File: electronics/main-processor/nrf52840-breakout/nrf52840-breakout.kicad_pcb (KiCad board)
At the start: 2 copper layers, 53 x 104.6 mm, 82 parts, among them J1 TBP02R2-381-03BE, J2 TBP02R2-381-02BE, J3 ST1W008S4AR1500, J4 TBP02R2-381-03BE, J5 USB4070-30-C_REVC5, J6 CONUFL001-SMD-T, J7 21992304, J8 Conn_01x04_Male, J9 TBP02R2-381-02BE, Q1 BSS214NW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

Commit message: up to pcb trace routing of circuit board, added boot and reset button
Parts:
- removed ?: , Micromod:M.2-CARD-E-22
- removed H1, H2: MountingHole, MountingHole:MountingHole_3.2mm_M3_Pad_Via
- removed JP1, JP2: SJ(Open), Jumper:SolderJumper-2_P1.3mm_Open_Pad1.0x1.5mm
- removed JP3, JP4: SJ(Clsd), Jumper:SolderJumper-2_P1.3mm_Bridged_Pad1.0x1.5mm
- added MP1: 9774025151R, 9774025151R:WE_9774025151R, F.Cu at (85.9, 110.6)
- added S2: RST, PTS636_SM43J_SMTR_LFS:SW_PTS636_SM43J_SMTR_LFS, F.Cu at (86.7, 96.8)
- added S3: BOOT, PTS636_SM43J_SMTR_LFS:SW_PTS636_SM43J_SMTR_LFS, F.Cu at (93.8, 93.2)
- C16: moved to F.Cu
- R11, R14: value 10K -> 5.1K
- R23: value 10K -> 20K
- moved R17 204.4 mm to (100.4, 107.3), turned to 0 degrees
- moved R24 196.5 mm to (96.0, 114.5), turned to -90 degrees
- moved D8 191.1 mm to (93.3, 127.7), turned to 0 degrees
- moved R16 188.9 mm to (100.4, 121.3), turned to 0 degrees
- moved U2 181.9 mm to (91.2, 68.0)
- moved C5 178.1 mm to (93.8, 86.8), turned to -90 degrees
- moved R6 177.1 mm to (73.0, 66.4)
- moved C1 176.5 mm to (90.0, 72.7), turned to 0 degrees
- moved R13 176.2 mm to (100.4, 123.3)
- moved J7 172.9 mm to (107.4, 114.6), turned to -90 degrees
- moved C4 172.0 mm to (94.6, 75.0)
- moved R22 158.9 mm to (100.4, 109.5)
- moved J9 123.6 mm to (74.5, 152.4)
- moved R14 110.4 mm to (80.8, 93.9), turned to 90 degrees
- moved U7 109.0 mm to (80.9, 123.0), turned to 90 degrees
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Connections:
- J5 pad A5: unconnected-(J5-PadA5) -> Net-(J5-PadA5)
- J5 pad B5: unconnected-(J5-PadB5) -> Net-(J5-PadB5)
- R11 pad 1: GND -> Net-(J5-PadA5)
- R11 pad 2: Net-(JP1-Pad1) -> GND
- R14 pad 2: Net-(JP2-Pad1) -> Net-(J5-PadB5)
- R23 pad 1: GND -> VBUS
- R23 pad 2: Net-(R23-Pad2) -> BATT_VIN/3
- R24 pad 1: GND -> BATT_VIN/3
- R24 pad 2: Net-(JP4-Pad1) -> GND
- U3 pad 1: Net-(JP1-Pad1) -> GND
- U3 pad 2: Net-(JP2-Pad1) -> GND
- U6 pad 1: Net-(R23-Pad2) -> +3.3V
- U6 pad 2: Net-(JP4-Pad1) -> +3.3V
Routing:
- net +12V: track 0.00 -> 32.4 mm
- net VBAT: track 0.00 -> 22.8 mm
- net Net-(C3-Pad1): track 0.00 -> 18.3 mm, vias 0 -> 2
- net Net-(D9-Pad2): track 0.00 -> 18.0 mm, vias 0 -> 2
- net +3.3V: track 0.00 -> 14.7 mm, vias 0 -> 2
- net GND: track 0.00 -> 14.7 mm, vias 0 -> 6
- net Net-(D1-Pad1): track 0.00 -> 14.6 mm
- net Net-(Q2-Pad3): track 0.00 -> 14.5 mm
- net Net-(C17-Pad2): track 0.00 -> 14.0 mm
- net BAT(+): track 0.00 -> 13.3 mm
- net Net-(L1-Pad2): track 0.00 -> 10.8 mm
- net Net-(C6-Pad1): track 0.00 -> 10.5 mm
- net Net-(J1-Pad2): track 0.00 -> 10.00 mm
- net Net-(R15-Pad1): track 0.00 -> 9.55 mm
- net D0: track 0.00 -> 9.21 mm
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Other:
- board size 53 x 104.6 mm -> 57.7 x 102.2 mm
- board text added: "12V"
- board text added: "5V"
- board text added: "Solar Charging"
- board text added: "Solar Fault"

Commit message: finalised board routing for first prototype
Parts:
- removed R23: 20K, Resistor_SMD:R_0805_2012Metric
- removed R24: 10K, Resistor_SMD:R_0805_2012Metric
- moved D8 32.7 mm to (81.2, 97.3), turned to 90 degrees
- moved C16 18.6 mm to (98.5, 104.2), turned to 180 degrees
- moved J8 9.35 mm to (90.0, 100.9), turned to -90 degrees
- moved R13 4.62 mm to (95.9, 124.2), turned to -90 degrees
- moved R16 3.76 mm to (98.0, 124.2), turned to -90 degrees
- moved J7 3.55 mm to (103.8, 114.5)
- moved MP1 3.55 mm to (82.3, 110.5)
- moved R22 2.55 mm to (97.8, 109.4)
- moved R17 2.55 mm to (97.8, 107.3)
- moved R28 2.52 mm to (97.9, 114.2)
- moved R31 2.51 mm to (97.9, 116.4)
- moved D2 1.93 mm to (106.1, 130.8)
- moved D3 1.93 mm to (106.1, 128.5)
- moved R7 1.93 mm to (109.8, 130.8)
- moved R8 1.93 mm to (109.8, 128.5)
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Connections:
- J5 pad B12: unconnected-(J5-PadB1) -> unconnected-(J5-PadB12)
- J5 pad B9: unconnected-(J5-PadB4) -> unconnected-(J5-PadB9)
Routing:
- net GND: track 14.7 -> 184.8 mm, vias 6 -> 24
- net VBAT: track 22.8 -> 165.8 mm
- net +3.3V: track 14.7 -> 77.8 mm, vias 2 -> 12
- net D1: track 5.15 -> 68.2 mm, vias 0 -> 2
- net I2C_SDA: track 0.00 -> 59.2 mm, vias 0 -> 4
- net GPIO5: track 0.00 -> 56.5 mm, vias 0 -> 2
- net SPI_CS: track 0.00 -> 53.9 mm, vias 0 -> 2
- net SPI_MOSI: track 0.00 -> 53.4 mm, vias 0 -> 4
- net I2C_SCL: track 0.00 -> 53.2 mm, vias 0 -> 4
- net SPI_SCK: track 0.00 -> 50.6 mm, vias 0 -> 2
- net SPI_MISO: track 0.00 -> 49.3 mm, vias 0 -> 2
- net D0: track 9.21 -> 57.1 mm, vias 0 -> 6
- net GPIO1: track 0.00 -> 43.8 mm, vias 0 -> 2
- net GPIO0: track 0.00 -> 43.5 mm, vias 0 -> 2
- net VBUS: track 7.86 -> 48.4 mm, vias 0 -> 2
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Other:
- board text added: "3.3V"
- board text added: "BAT(+)"
- board text added: "BAT(-)"
- board text added: "Charging"
- board text added: "Fault"
- board text added: "GND"
- board text added: "Harvey Bates Sept 2022"
- board text added: "Neg"
- board text added: "RST"
- board text removed: "Solar Charging"
- board text removed: "Solar Fault"

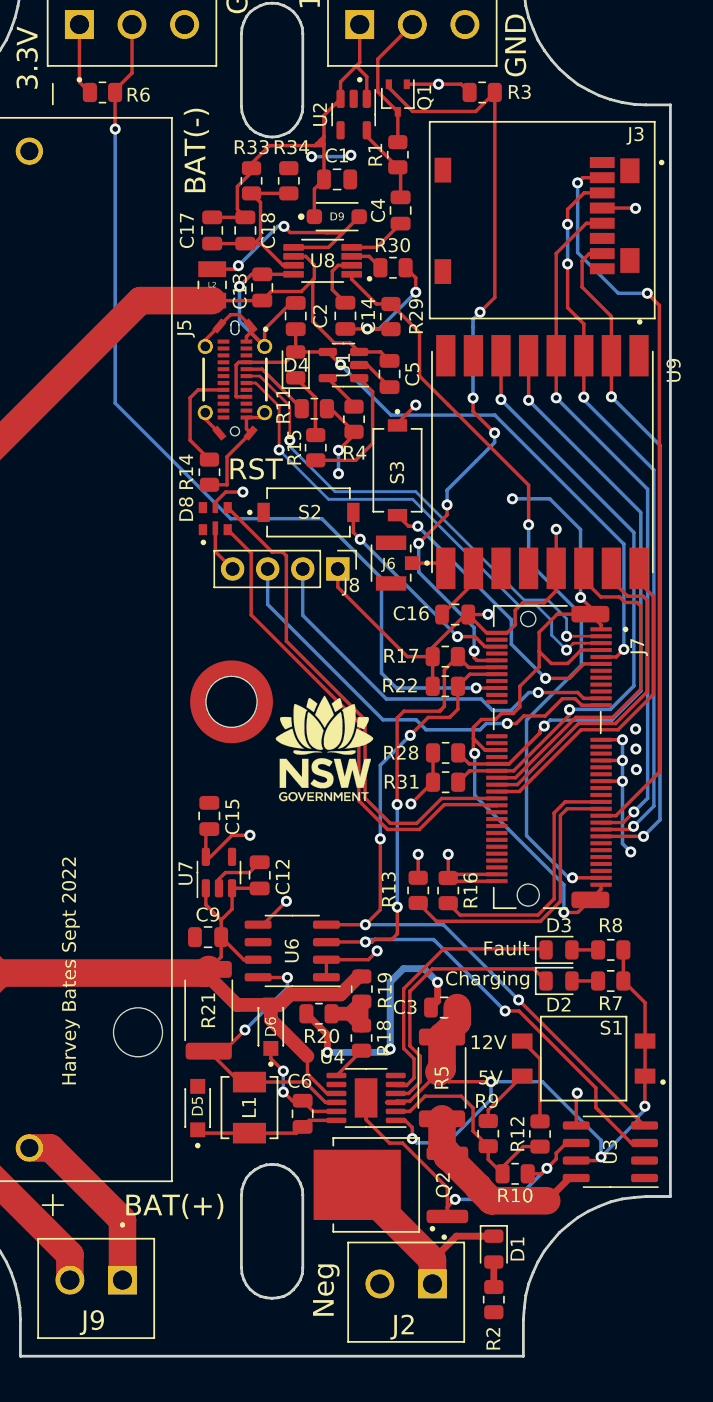
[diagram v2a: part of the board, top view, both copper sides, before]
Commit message: added basic feather m0 node. Features: no solar, d-cell battery, 12 V boost, sd-card, SDI12, i2c, wind speed and dir, reverse polarity protection and indicator
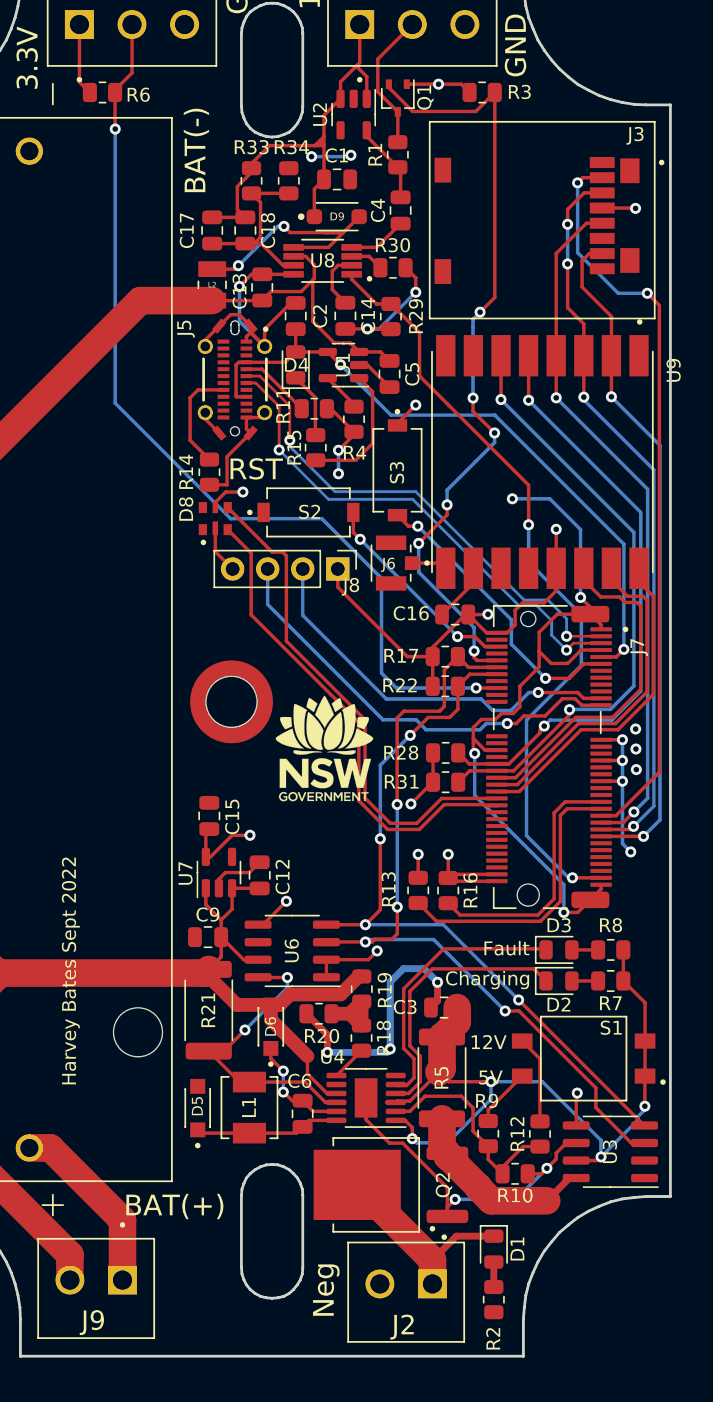
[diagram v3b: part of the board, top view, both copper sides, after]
